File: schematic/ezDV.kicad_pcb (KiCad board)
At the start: 4 copper layers, 72.4 x 90.2 mm, 53 parts, among them J1 Radio_Jack, J2 User_Jack, J3 nanoESP32-S3-Left, J4 nanoESP32-S3-Right, Q1 MBT3904DW1T1, Q2 MBT3904DW1T1, Q3 MBT3904DW1T1, SW1 PTT_Button, SW2 Mode_Button, SW3 Vol_Up_Button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

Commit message: Rename SM1000neo to ezDV.
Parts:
- U1: footprint SM1000neo:IC_ADS125H01IRHBT -> ezDV:IC_ADS125H01IRHBT
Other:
- board text added: "ezDV Dev Platform v0.1 https://github.com/tmiw/ezDV"
- board text removed: "SM1000neo Dev Platform v0.1 https://github.com/tmiw/SM1000neo"
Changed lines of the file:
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@@
     (add_net User_Jack_Speaker)
   )
-  (module SM1000neo:IC_ADS125H01IRHBT (layer F.Cu)
+  (module ezDV:IC_ADS125H01IRHBT (layer F.Cu)
     (at 91.44 3.81 270)
     (attr smd)
@@
     )
   )
-  (gr_text "SM1000neo Dev Platform v0.1\nhttps://github.com/tmiw/SM1000neo" (at 124.46 -19.05 90) (layer F.SilkS)
+  (gr_text "ezDV Dev Platform v0.1\nhttps://github.com/tmiw/ezDV" (at 124.46 -19.05 90) (layer F.SilkS)
     (effects (font (size 1 1) (thickness 0.15)))
   )

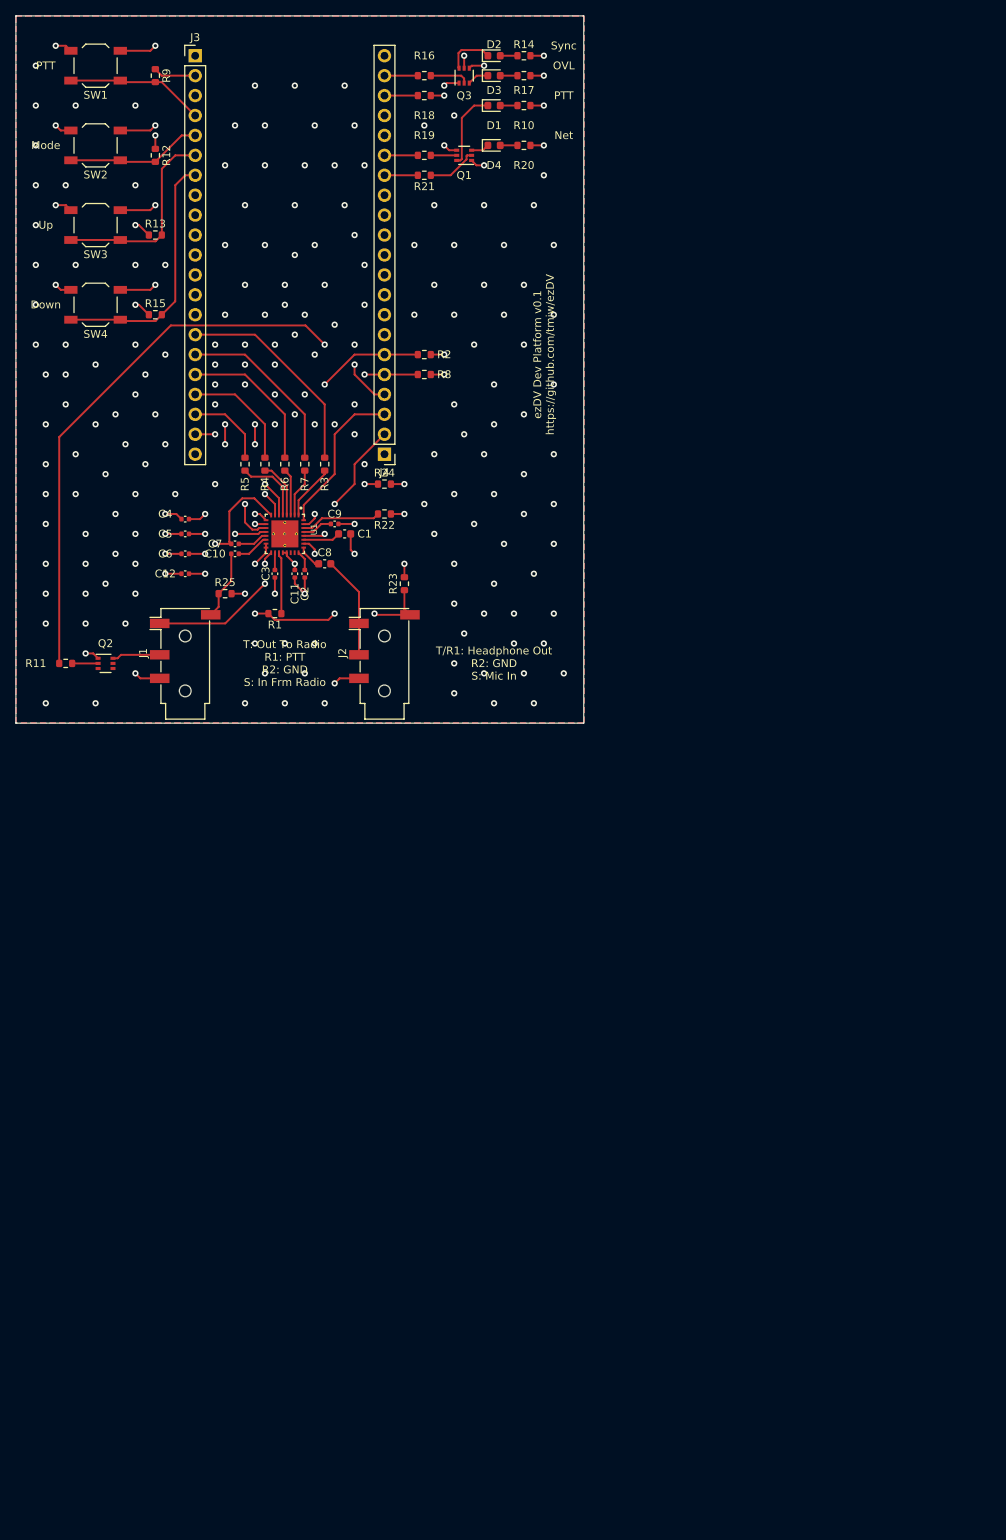
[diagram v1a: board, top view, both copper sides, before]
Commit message: Recreated dev platform PCB from scratch;
1. Swapped MFP4 and Reset for TLV320 for ease of routing. (#10)
2. Added vias around outside edge of board. (#1)
3. Added mounting holes for the dev board. (#5)
4. Moved silkscreen labels to improve readability. (#7)
5. Routed sensitive audio traces in inner layer and surrounded by ground vias/planes. (#10)
6. Set mic input capacitor values to same as used on TLV320 EVM to help with noise. (#10)
7. Replaced some parts with 0402 equivalents to help with positioning closer to TLV320. (#10)
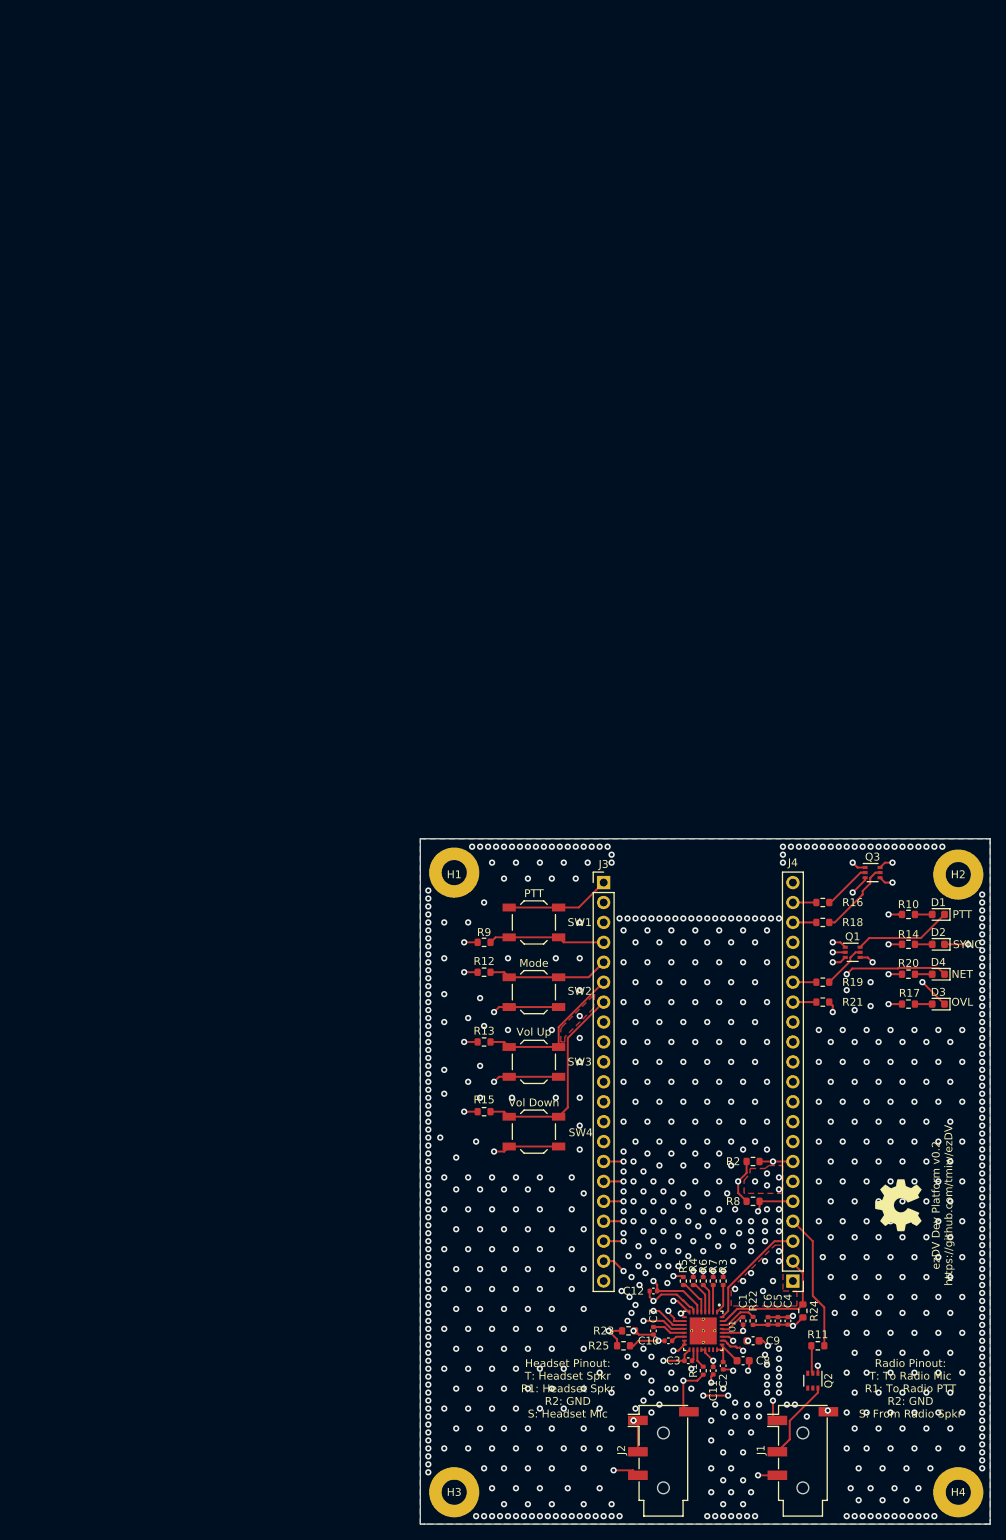
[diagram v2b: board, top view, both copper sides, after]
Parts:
- added H1: MountingHole_Pad, MountingHole:MountingHole_3.2mm_M3_Pad, F.Cu at (113.0, 47.0)
- added H2: MountingHole_Pad, MountingHole:MountingHole_3.2mm_M3_Pad, F.Cu at (177.3, 47.2)
- added H3: MountingHole_Pad, MountingHole:MountingHole_3.2mm_M3_Pad, F.Cu at (113.0, 126.0)
- added H4: MountingHole_Pad, MountingHole:MountingHole_3.2mm_M3_Pad, F.Cu at (177.3, 126.0)
- added REF**: OSHW-Symbol_6.7x6mm_SilkScreen, Symbol:OSHW-Symbol_6.7x6mm_SilkScreen, F.Cu at (169.7, 89.4)
- C10, C7: value 0.1uF -> 0.47uF
- R1: value 2.7K -> 1K; footprint Resistor_SMD:R_0603_1608Metric -> Resistor_SMD:R_0402_1005Metric
- R10, R17: value 100 -> 50
- R22, R3, R4, R5, R6, R7: footprint Resistor_SMD:R_0603_1608Metric -> Resistor_SMD:R_0402_1005Metric
- moved D3 131.2 mm to (174.8, 63.8), turned to 180 degrees
- moved R11 129.5 mm to (159.4, 107.3), turned to 0 degrees
- moved J1 128.5 mm to (157.5, 120.7)
- moved Q2 128.4 mm to (158.8, 111.8), turned to 270 degrees
- moved R17 128.1 mm to (170.9, 63.8), turned to 180 degrees
- moved C4 127.9 mm to (155.6, 104.1), turned to 90 degrees
- moved D2 126.7 mm to (174.8, 56.1), turned to 180 degrees
- moved C5 125.6 mm to (154.3, 104.1), turned to 90 degrees
- moved R14 123.4 mm to (170.9, 56.1), turned to 180 degrees
- moved C6 122.8 mm to (153.0, 104.1), turned to 90 degrees
- moved SW1 122.7 mm to (123.2, 53.3)
- moved SW2 121.6 mm to (123.2, 62.2), turned to 0 degrees
- moved SW3 120.4 mm to (123.2, 71.1), turned to 0 degrees
- moved D4 119.9 mm to (174.8, 59.9), turned to 180 degrees
- moved SW4 119.3 mm to (123.2, 80.0), turned to 0 degrees
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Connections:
- J3 pad 20: GPIO12_TLV320_RESET -> GPIO12_TLV320_MFP4
- J4 pad 2: GPIO13_TLV320_MFP4 -> GPIO13_TLV320_RESET
- J4 pad 6: GPIO48_TLV320_SCL -> Net-(J4-Pad6)
- J4 pad 7: GPIO45 -> GPIO45_TLV320_SCL
- R2 pad 2: GPIO48_TLV320_SCL -> GPIO45_TLV320_SCL
- R24 pad 1: GPIO12_TLV320_RESET -> GPIO13_TLV320_RESET
- U1 pad 11: GPIO13_TLV320_MFP4 -> GPIO12_TLV320_MFP4
- U1 pad 31: GPIO12_TLV320_RESET -> GPIO13_TLV320_RESET
- U1 pad 9: GPIO48_TLV320_SCL -> GPIO45_TLV320_SCL
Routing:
- net GPIO21_PTT_OUT: track 80.6 -> 17.5 mm, vias 2 -> 0
- net GPIO48_TLV320_SCL: track 40.3 -> 0.00 mm, vias 4 -> 0
- net GPIO12_TLV320_RESET: track 35.8 -> 0.00 mm, vias 3 -> 0
- net GPIO45_TLV320_SCL: track 0.00 -> 32.6 mm, vias 0 -> 2
- net GPIO13_TLV320_MFP4: track 32.1 -> 0.00 mm, vias 2 -> 0
- net Radio_Jack_Mic: track 8.86 -> 30.3 mm, vias 0 -> 2
- net Net-(D3-Pad1): track 2.77 -> 23.1 mm, vias 0 -> 2
- net Radio_Jack_Speaker: track 31.3 -> 11.4 mm
- net GPIO13_TLV320_RESET: track 0.00 -> 17.2 mm
- net TLV320_IN_DETECT: track 48.1 -> 31.9 mm, vias 4 -> 3
- net Net-(D4-Pad1): track 2.33 -> 17.4 mm, vias 0 -> 2
- net GPIO12_TLV320_MFP4: track 0.00 -> 14.5 mm, vias 0 -> 2
- net Net-(D2-Pad1): track 6.17 -> 20.0 mm, vias 0 -> 2
- net GPIO47_TLV320_SDA: track 44.4 -> 33.1 mm, vias 4 -> 2
- net User_Jack_Speaker: track 13.1 -> 22.9 mm, vias 0 -> 4
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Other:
- board size 72.4 x 90.2 mm -> 72.6 x 87.4 mm
- board text added: "Headset Pinout: T: Headset Spkr R1: Headset Spkr R2: GND S: Headset Mic"
- board text added: "NET"
- board text added: "Radio Pinout: T: To Radio Mic R1: To Radio PTT R2: GND S: From Radio Spkr"
- board text added: "SYNC"
- board text added: "Vol Down"
- board text added: "Vol Up"
- board text added: "ezDV Dev Platform v0.2 https://github.com/tmiw/ezDV"
- board text removed: "Down"
- board text removed: "Net"
- board text removed: "Sync"
- board text removed: "T/R1: Headphone Out R2: GND S: Mic In"
- board text removed: "T: Out To Radio R1: PTT R2: GND S: In Frm Radio"
- board text removed: "Up"
- board text removed: "ezDV Dev Platform v0.1 https://github.com/tmiw/ezDV"
